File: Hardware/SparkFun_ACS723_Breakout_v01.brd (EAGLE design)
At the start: 24.1 x 15.2 mm, 19 parts, among them U1 ACS723ACS723LLCTR-05AB-T2

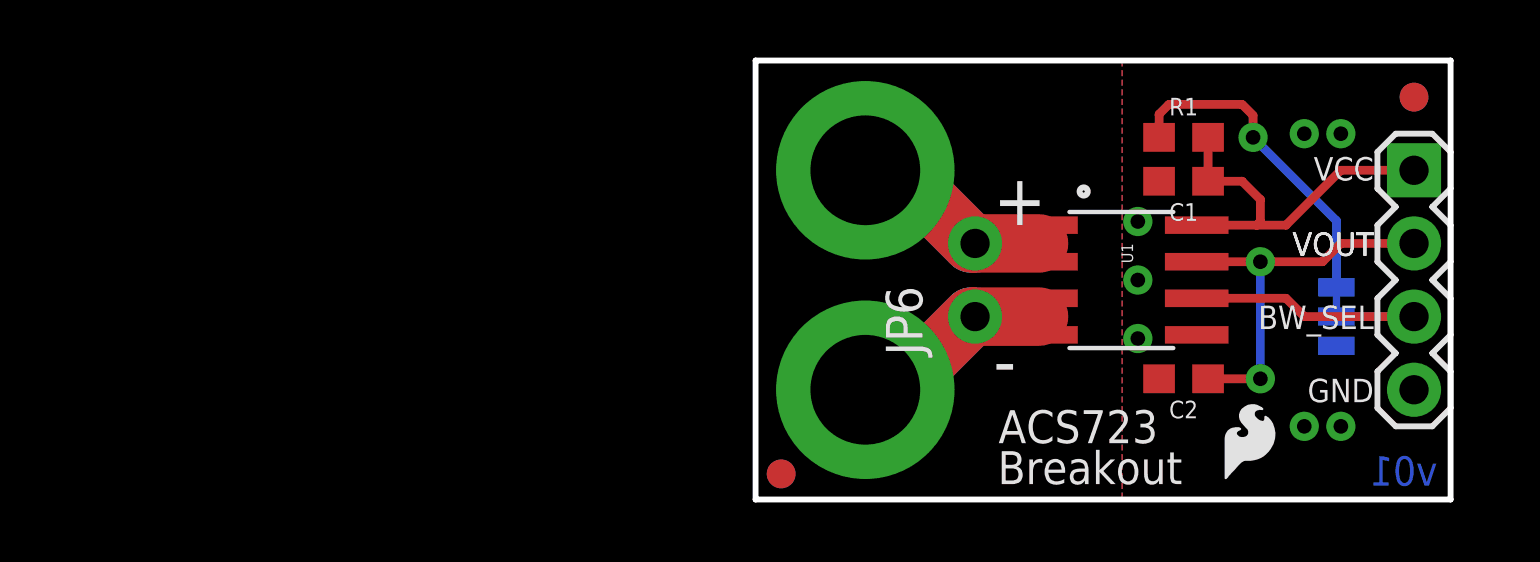
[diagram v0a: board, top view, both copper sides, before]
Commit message: Post Eng. Review changes
-added standoff
-removed BW_SEL through-hole
-moved some silk around
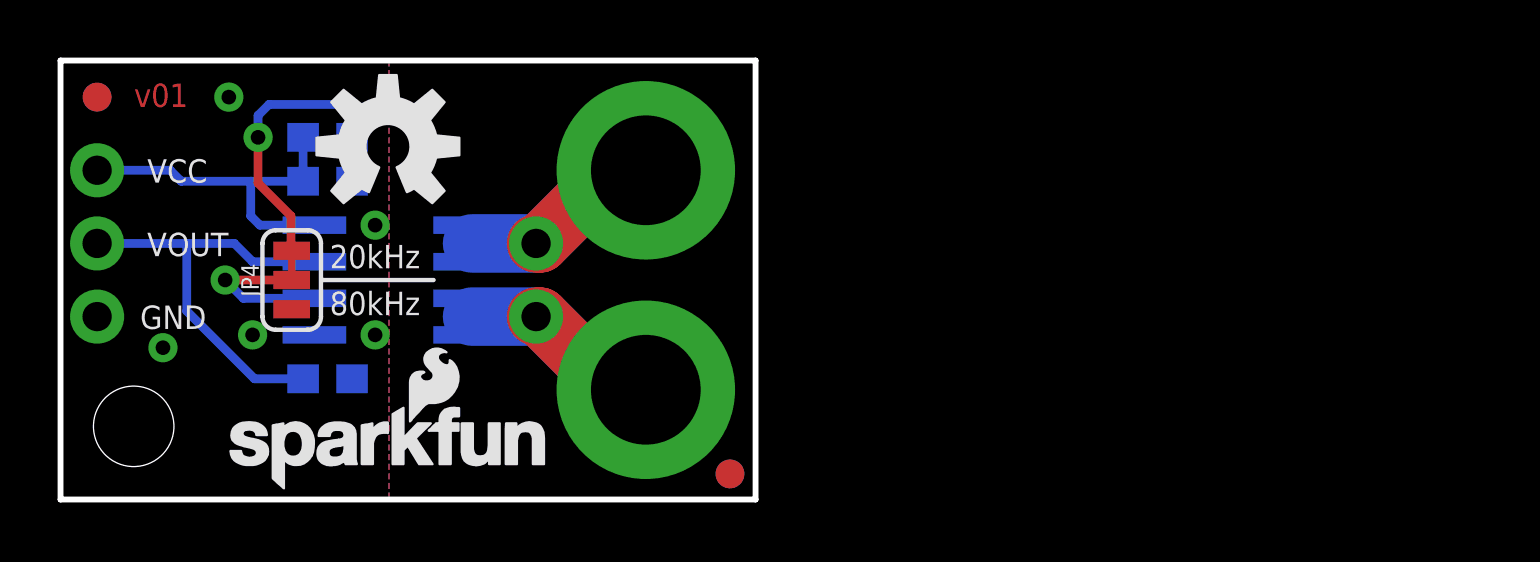
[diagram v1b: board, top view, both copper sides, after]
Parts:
- added J1: 455-1750-1-ND, SparkFun-Connectors:1X03
- JP3: value (none) -> STAND-OFFTIGHTER_(0.11_INCH_DIA); device SparkFun-Connectors:1X04 -> Testing:STAND-OFF-TIGHTER
- U1: value ACS723ACS723LLCTR-05AB-T2 -> ACS723; device SparkFun-IC-Power:SO08 -> SparkFun-Sensors:SO08
- moved FD3 45.7 mm to (-22.9, 14.0), flipped to the top
- moved FD4 45.7 mm to (-22.9, 14.0), flipped to the bottom
- moved JP3 45.3 mm to (-21.6, 2.54), flipped to the bottom, turned to 0 degrees
- moved LOGO2 37.5 mm to (-18.7, -0.11), flipped to the top
- moved JP4 36.3 mm to (-16.1, 7.62), flipped to the top
- moved FRAME1 33.0 mm to (16.5, -11.4), flipped to the bottom
- moved C1 29.7 mm to (-14.9, 11.0), flipped to the bottom
- moved C2 29.7 mm to (-14.9, 4.19), flipped to the bottom
- moved R1 29.7 mm to (-14.9, 12.6), flipped to the bottom
- moved U$6 27.9 mm to (-9.53, 11.6), flipped to the bottom
- moved U1 25.4 mm to (-12.7, 7.62), flipped to the bottom
- moved U$3 25.1 mm to (-12.8, 12.3), flipped to the top
- moved U$5 24.6 mm to (-12.3, 2.35), flipped to the top
- moved JP6 15.2 mm to (-7.62, 6.35), flipped to the bottom
- moved U$1 10.2 mm to (5.08, -14.0), flipped to the bottom
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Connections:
- net BW_SEL: no longer JP3.3
- net GND: now also J1.3; no longer JP3.4
- net N$1: now also J1.2; no longer JP3.2
- net VCC: now also J1.1; no longer JP3.1
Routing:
- net BW_SEL: track 10.5 -> 5.67 mm, vias 0 -> 1
- net N$3: track 11.5 -> 9.55 mm
- net N$1: track 13.7 -> 15.2 mm, vias 2 -> 0
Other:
- board text added: "Current Sensor"
- board text added: "IP+"
- board text added: "IP-"
- board text removed: "+"
- board text removed: "-"
- board text removed: "BW_SEL"
- board text removed: "Breakout"
- board text removed: "Max Current Sensing: 5A"

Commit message: final touches for checklist
-moved silk
-moved headers so they're on 100mil grid
- Added measures
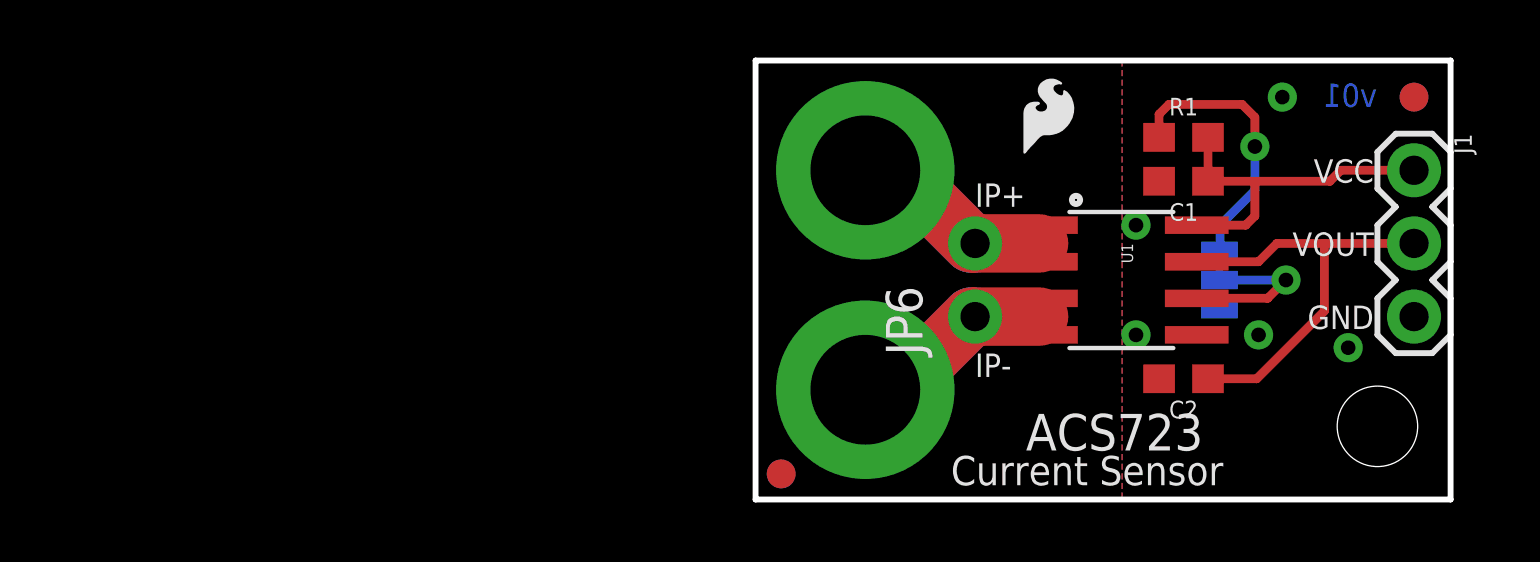
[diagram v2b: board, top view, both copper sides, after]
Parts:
- removed LOGO2: SFE_LOGO_NAME.1_INCH, SparkFun-Aesthetics:SFE_LOGO_NAME_.1
- removed U$3: (no value), SparkFun-Aesthetics:OSHW-LOGO-M
- removed U$5, U$6: (no value), SparkFun-Aesthetics:SFE_LOGO_FLAME_.1
- added LOGO1: SFE_LOGO_FLAME.1_INCH, SparkFun-Aesthetics:SFE_LOGO_FLAME_.1
- added LOGO3: SFE_LOGO_NAME_FLAME.1_INCH, SparkFun-Aesthetics:SFE_LOGO_NAME_FLAME_.1
- added LOGO4: OSHW-LOGOM, SparkFun-Aesthetics:OSHW-LOGO-M
- moved FD3 45.7 mm to (22.9, 14.0), flipped to the bottom
- moved FD4 45.7 mm to (22.9, 14.0), flipped to the top
- moved J1 45.7 mm to (22.9, 11.4), flipped to the top
- moved JP3 43.2 mm to (21.6, 2.54), flipped to the top
- moved FRAME1 33.0 mm to (-16.5, -11.4), flipped to the top
- moved JP4 32.2 mm to (16.1, 7.62), flipped to the bottom
- moved C1 29.7 mm to (14.9, 11.0), flipped to the top
- moved C2 29.7 mm to (14.9, 4.19), flipped to the top
- moved R1 29.7 mm to (14.9, 12.6), flipped to the top
- moved U1 25.4 mm to (12.7, 7.62), flipped to the top
- moved JP6 15.2 mm to (7.62, 6.35), flipped to the top
- moved U$1 10.2 mm to (-5.08, -14.0), flipped to the top
- moved JP1 7.62 mm to (3.81, 11.4), flipped to the top
- moved JP2 7.62 mm to (3.81, 3.81), flipped to the top
- moved FD2 1.78 mm to (0.89, 0.89), flipped to the top
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
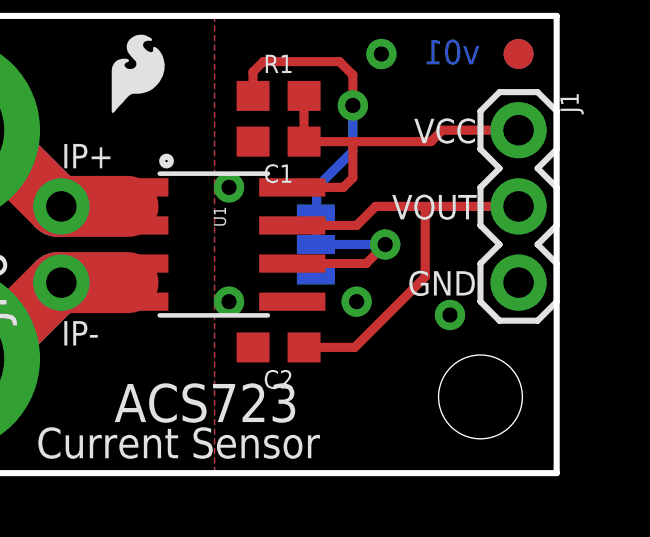
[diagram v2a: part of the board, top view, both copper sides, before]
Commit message: v01 Proto checklist issues fixed
-added BW_SEL note in SCH
-Removed redundant via by GND through-hole
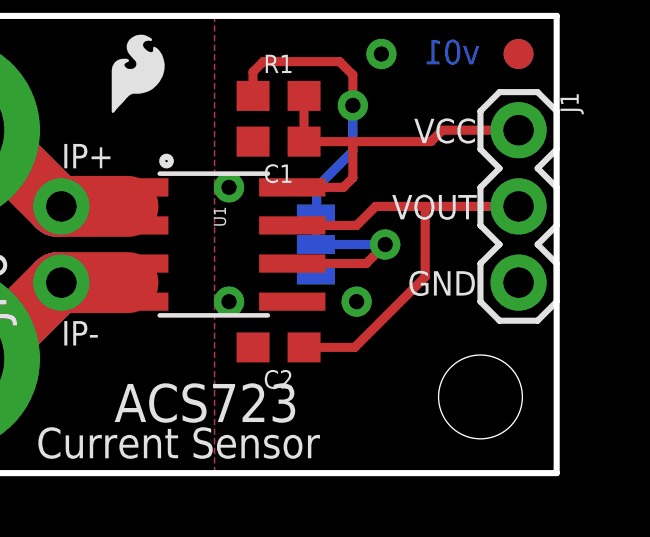
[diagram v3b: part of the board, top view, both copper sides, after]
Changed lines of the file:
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@@
 <setting verticaltext="up"/>
 </settings>
-<grid distance="0.1" unitdist="inch" unit="inch" style="lines" multiple="1" display="yes" altdistance="0.0025" altunitdist="inch" altunit="inch"/>
+<grid distance="0.05" unitdist="inch" unit="inch" style="lines" multiple="1" display="yes" altdistance="0.005" altunitdist="inch" altunit="inch"/>
 <layers>
 <layer number="1" name="Top" color="4" fill="1" visible="yes" active="yes"/>
@@
 <layer number="20" name="Dimension" color="15" fill="1" visible="yes" active="yes"/>
 <layer number="21" name="tPlace" color="16" fill="1" visible="yes" active="yes"/>
-<layer number="22" name="bPlace" color="14" fill="1" visible="yes" active="yes"/>
+<layer number="22" name="bPlace" color="14" fill="1" visible="no" active="yes"/>
 <layer number="23" name="tOrigins" color="15" fill="1" visible="yes" active="yes"/>
-<layer number="24" name="bOrigins" color="15" fill="1" visible="yes" active="yes"/>
-<layer number="25" name="tNames" color="7" fill="1" visible="no" active="yes"/>
+<layer number="24" name="bOrigins" color="15" fill="1" visible="no" active="yes"/>
+<layer number="25" name="tNames" color="7" fill="1" visible="yes" active="yes"/>
 <layer number="26" name="bNames" color="7" fill="1" visible="no" active="yes"/>
 <layer number="27" name="tValues" color="7" fill="1" visible="no" active="yes"/>
@@
 <layer number="43" name="vRestrict" color="2" fill="10" visible="no" active="yes"/>
 <layer number="44" name="Drills" color="7" fill="1" visible="no" active="yes"/>
-<layer number="45" name="Holes" color="7" fill="1" visible="yes" active="yes"/>
+<layer number="45" name="Holes" color="7" fill="1" visible="no" active="yes"/>
 <layer number="46" name="Milling" color="3" fill="1" visible="no" active="yes"/>
 <layer number="47" name="Measures" color="7" fill="1" visible="no" active="yes"/>
 <layer number="48" name="Document" color="7" fill="1" visible="no" active="yes"/>
-<layer number="49" name="Reference" color="13" fill="1" visible="yes" active="yes"/>
+<layer number="49" name="Reference" color="13" fill="1" visible="no" active="yes"/>
 <layer number="50" name="dxf" color="7" fill="1" visible="no" active="yes"/>
-<layer number="51" name="tDocu" color="6" fill="1" visible="yes" active="yes"/>
+<layer number="51" name="tDocu" color="6" fill="1" visible="no" active="yes"/>
 <layer number="52" name="bDocu" color="7" fill="1" visible="no" active="yes"/>
 <layer number="53" name="tGND_GNDA" color="7" fill="9" visible="no" active="no"/>
@@
 <layer number="225" name="225bmp" color="7" fill="1" visible="no" active="yes"/>
 <layer number="226" name="226bmp" color="7" fill="1" visible="no" active="yes"/>
-<layer number="227" name="LAYER_2" color="11" fill="1" visible="yes" active="yes"/>
-<layer number="228" name="LAYER_3" color="10" fill="1" visible="yes" active="yes"/>
-<layer number="229" name="LAYER_4" color="14" fill="1" visible="yes" active="yes"/>
-<layer number="230" name="LAYER_5" color="12" fill="1" visible="yes" active="yes"/>
-<layer number="231" name="LAYER_6" color="9" fill="1" visible="yes" active="yes"/>
+<layer number="227" name="LAYER_2" color="11" fill="1" visible="no" active="yes"/>
+<layer number="228" name="LAYER_3" color="10" fill="1" visible="no" active="yes"/>
+<layer number="229" name="LAYER_4" color="14" fill="1" visible="no" active="yes"/>
+<layer number="230" name="LAYER_5" color="12" fill="1" visible="no" active="yes"/>
+<layer number="231" name="LAYER_6" color="9" fill="1" visible="no" active="yes"/>
 <layer number="232" name="Eagle3D_PG2" color="7" fill="1" visible="no" active="yes"/>
 <layer number="233" name="Eagle3D_PG3" color="7" fill="1" visible="no" active="yes"/>
@@
 <contactref element="JP4" pad="1"/>
 <contactref element="C2" pad="2"/>
-<via x="20.574" y="5.2705" extent="1-16" drill="0.508"/>
 <via x="13.208" y="9.525" extent="1-16" drill="0.508"/>
 <via x="13.208" y="5.715" extent="1-16" drill="0.508"/>

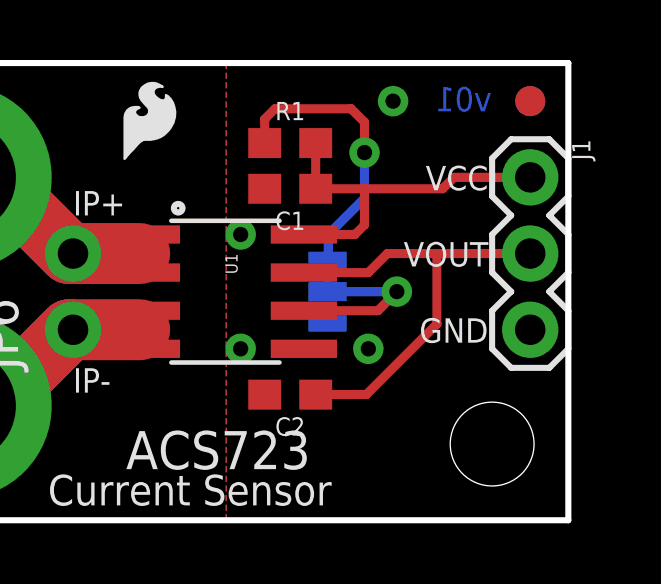
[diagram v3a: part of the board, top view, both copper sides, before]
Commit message: changes after v01
-adjusted pin label font form 32mil to 40mil
-changed standoff to a part that lives in the sparkfun-hardware lbr
-adjusted some spacing on silk labels
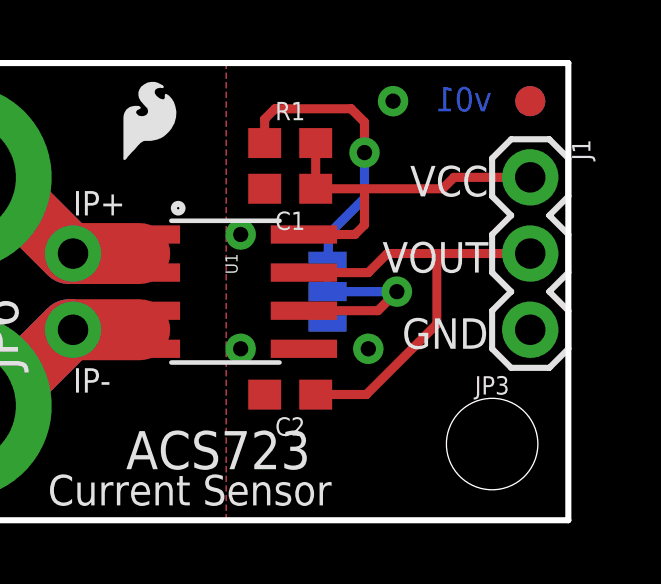
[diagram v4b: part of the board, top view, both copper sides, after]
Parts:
- JP3: value STAND-OFFTIGHTER_(0.11_INCH_DIA) -> STAND-OFFTIGHT; device Testing:STAND-OFF-TIGHTER -> SparkFun-Hardware:STAND-OFF-TIGHT
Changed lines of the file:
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@@
 <wire x1="24.13" y1="15.24" x2="24.13" y2="0" width="0.2032" layer="20"/>
 <wire x1="24.13" y1="0" x2="0" y2="0" width="0.2032" layer="20"/>
-<text x="21.463" y="11.811" size="0.8128" layer="21" font="vector" ratio="15" rot="R180">VCC</text>
-<text x="21.463" y="6.731" size="0.8128" layer="21" font="vector" ratio="15" rot="R180">GND</text>
+<text x="21.463" y="11.811" size="1.016" layer="21" font="vector" ratio="15" rot="R180">VCC</text>
+<text x="21.463" y="6.731" size="1.016" layer="21" font="vector" ratio="15" rot="R180">GND</text>
 <text x="9.3853" y="1.7018" size="1.27" layer="21" font="vector" ratio="15">ACS723</text>
 <text x="21.5773" y="13.6271" size="0.8128" layer="16" font="vector" ratio="15" rot="MR0">v01</text>
 <dimension x1="0" y1="19.05" x2="24.13" y2="19.05" x3="12.065" y3="20.32" textsize="1.778" textratio="15" layer="47" unit="inch" visible="yes"/>
 <text x="13.9446" y="-11.4808" size="1.778" layer="51" font="vector">Pete Dokter</text>
-<text x="19.03221875" y="11.813540625" size="0.8128" layer="22" font="vector" ratio="15" rot="MR180">VCC</text>
-<text x="21.463" y="9.271" size="0.8128" layer="21" font="vector" ratio="15" rot="R180">VOUT</text>
-<text x="18.3007" y="9.260840625" size="0.8128" layer="22" font="vector" ratio="15" rot="MR180">VOUT</text>
-<text x="19.06778125" y="6.733540625" size="0.8128" layer="22" font="vector" ratio="15" rot="MR180">GND</text>
+<text x="18.6182" y="11.940540625" size="1.016" layer="22" font="vector" ratio="15" rot="MR180">VCC</text>
+<text x="21.463" y="9.271" size="1.016" layer="21" font="vector" ratio="15" rot="R180">VOUT</text>
+<text x="17.6784" y="9.387840625" size="1.016" layer="22" font="vector" ratio="15" rot="MR180">VOUT</text>
+<text x="18.6182" y="6.860540625" size="1.016" layer="22" font="vector" ratio="15" rot="MR180">GND</text>
 <text x="13.4366" y="-14.0208" size="1.778" layer="51" font="vector">Eric Orosel</text>
 <text x="7.62" y="10.16" size="0.8128" layer="21" font="vector" ratio="15">IP+</text>
@@
 <attribute name="PROD_ID" value="XXX-00000" x="22.86" y="11.43" size="1.778" layer="27" font="vector" ratio="15" rot="R270" display="off"/>
 </element>
-<element name="JP3" library="Testing" package="STAND-OFF-TIGHTER" value="STAND-OFFTIGHTER_(0.11_INCH_DIA)" x="21.59" y="2.54"/>
+<element name="JP3" library="SparkFun-Hardware" package="STAND-OFF-TIGHT" value="STAND-OFFTIGHT" x="21.59" y="2.54"/>
 <element name="LOGO1" library="SparkFun-Aesthetics" package="SFE_LOGO_FLAME_.1" value="SFE_LOGO_FLAME.1_INCH" x="9.017" y="11.684"/>
 <element name="LOGO3" library="SparkFun-Aesthetics" package="SFE_LOGO_NAME_FLAME_.1" value="SFE_LOGO_NAME_FLAME.1_INCH" x="18.7325" y="0.254" rot="MR0"/>
